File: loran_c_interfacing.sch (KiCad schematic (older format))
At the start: 17 parts, among them P401 SPI Bus A, P402 SPI Bus B, U103 74AC14, U401 74AC14, U402 74AC14

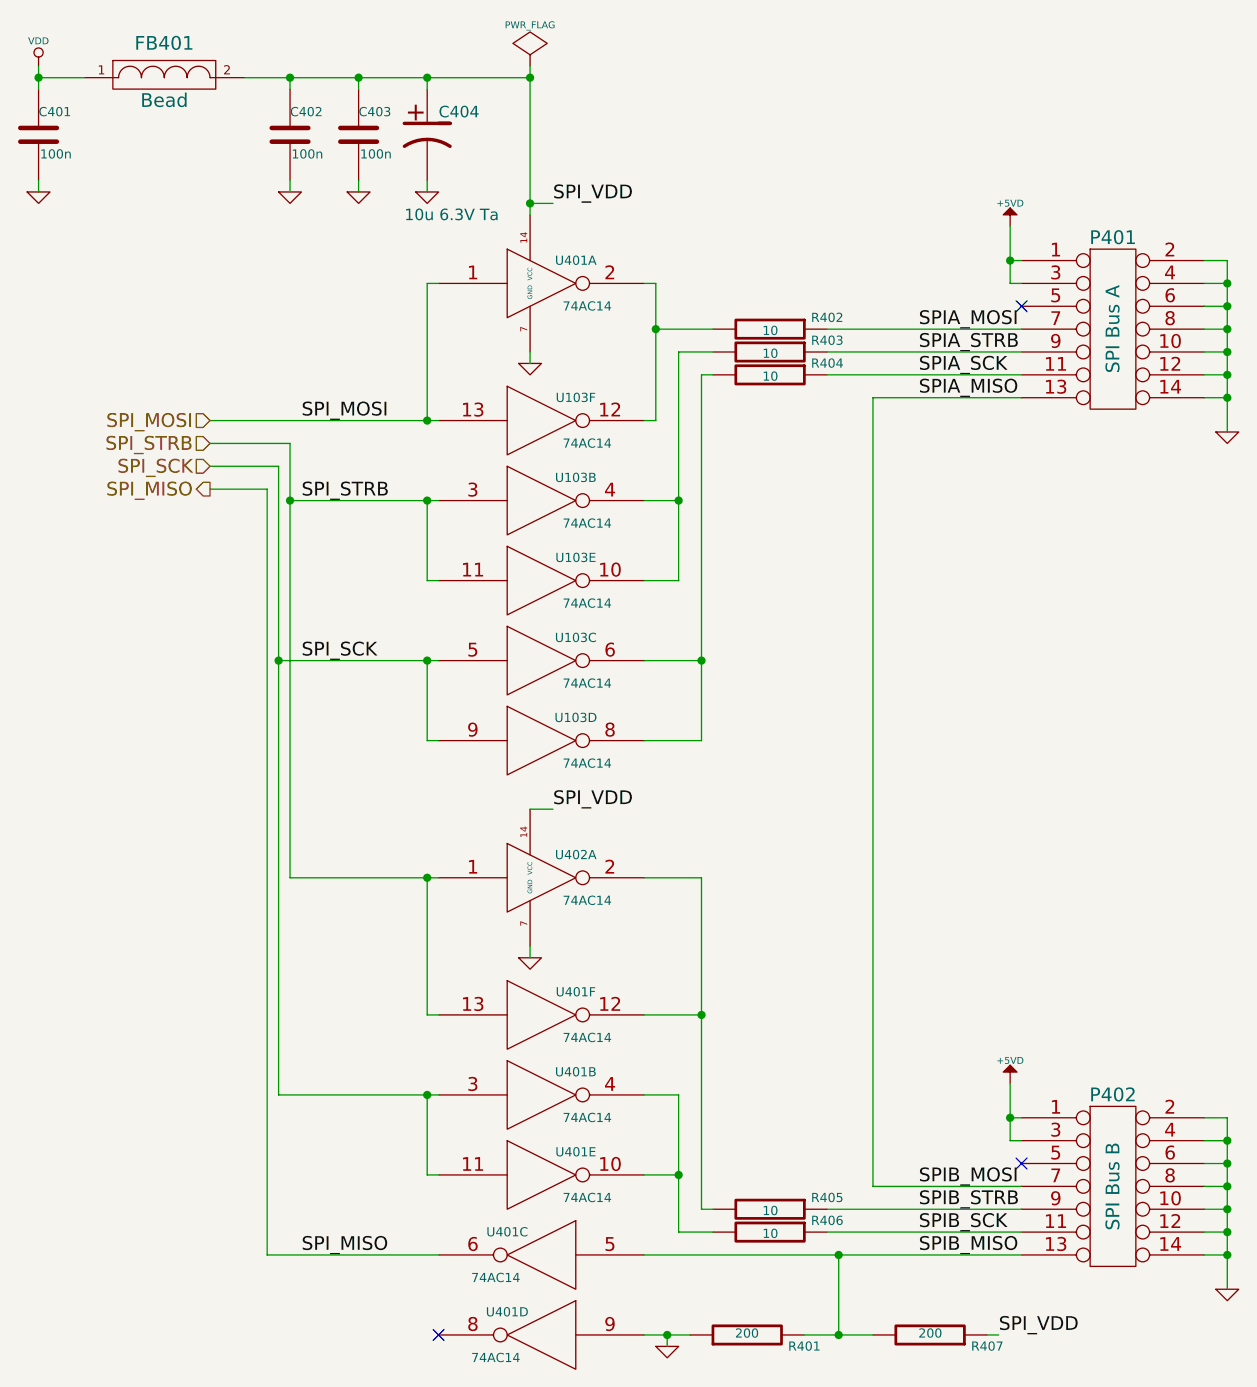
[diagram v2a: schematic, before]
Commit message: Fix: broken annotation, sheet numbers, incorrect 74AC14 package
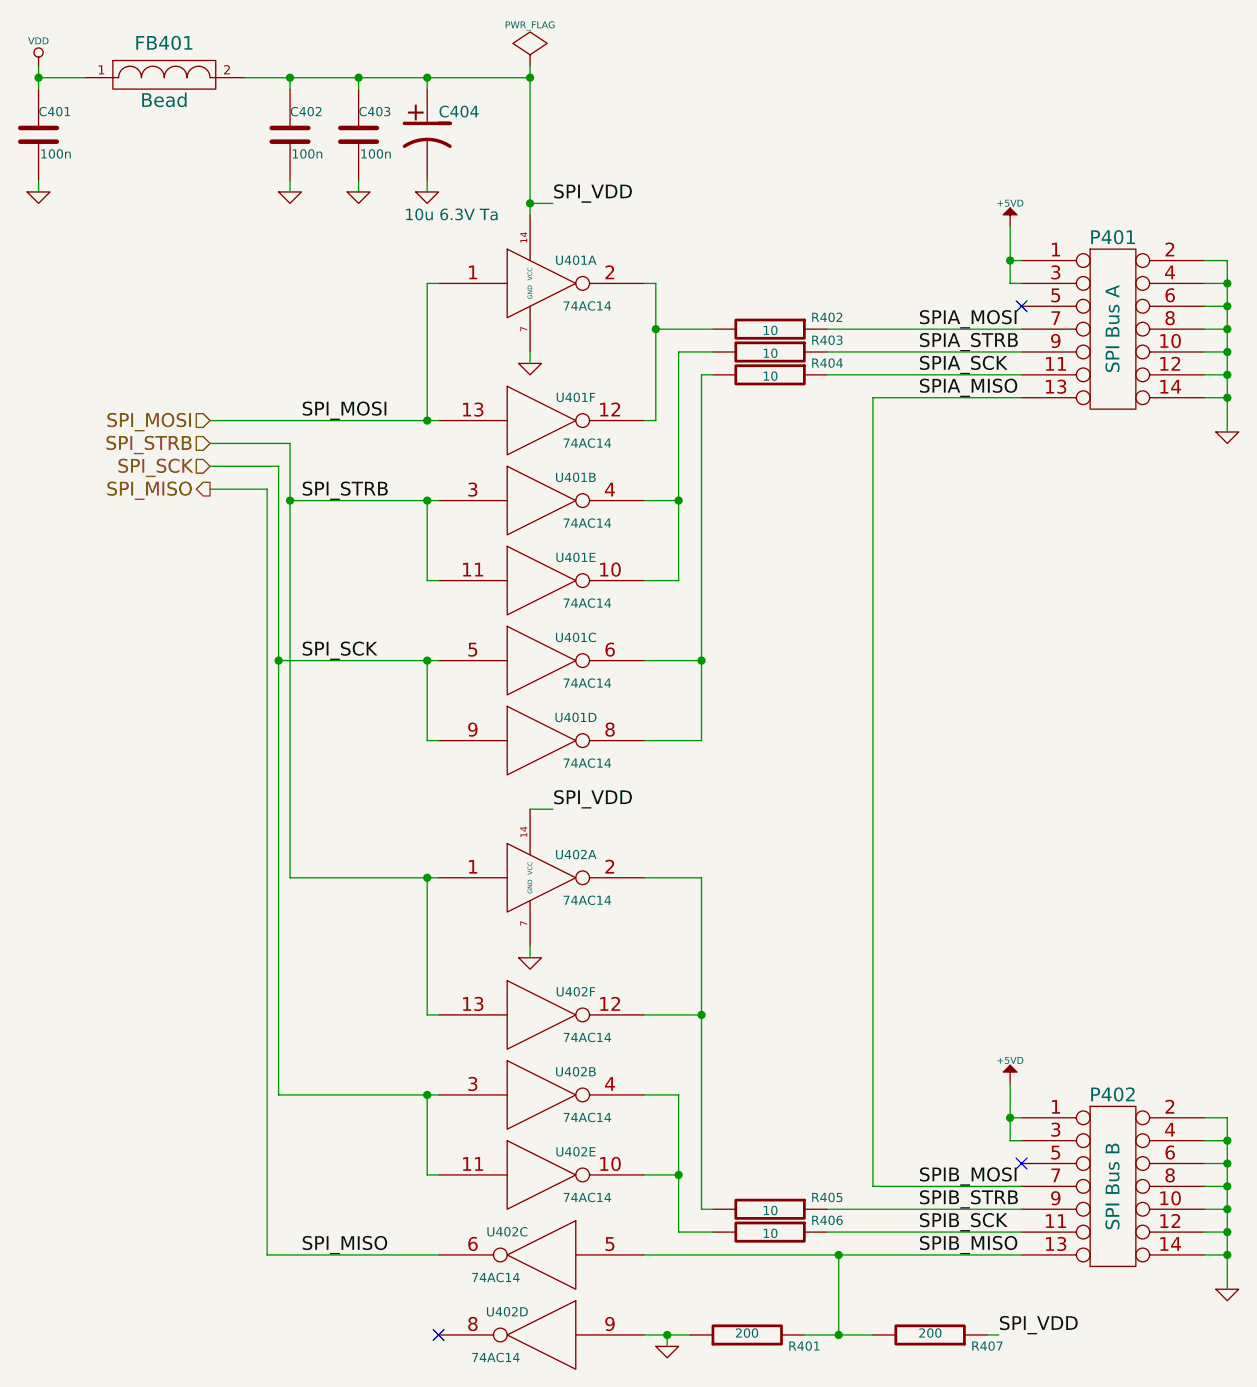
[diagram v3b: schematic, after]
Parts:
- renumbered U103 to U401, U401 to U402
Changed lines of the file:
@@
 $Descr A4 11693 8268
 encoding utf-8
-Sheet 3 7
+Sheet 4 7
 Title "SPI interface"
 Date ""
@@
 SPI_VDD
 $Comp
-L 74HC14 U103
+L 74HC14 U401
 U 6 1 52DD85CF
 P 5600 2300
-F 0 "U103" H 5750 2400 40  0000 C CNN
+F 0 "U401" H 5750 2400 40  0000 C CNN
 F 1 "74AC14" H 5800 2200 40  0000 C CNN
 F 2 "w_smd_dil:so-16" H 5600 2300 60  0001 C CNN
@@
 $EndComp
 $Comp
-L 74HC14 U103
+L 74HC14 U401
 U 2 1 52DD85E6
 P 5600 2650
-F 0 "U103" H 5750 2750 40  0000 C CNN
+F 0 "U401" H 5750 2750 40  0000 C CNN
 F 1 "74AC14" H 5800 2550 40  0000 C CNN
 F 2 "w_smd_dil:so-16" H 5600 2650 60  0001 C CNN
@@
 $EndComp
 $Comp
-L 74HC14 U103
+L 74HC14 U401
 U 5 1 52DD85F1
 P 5600 3000
-F 0 "U103" H 5750 3100 40  0000 C CNN
+F 0 "U401" H 5750 3100 40  0000 C CNN
 F 1 "74AC14" H 5800 2900 40  0000 C CNN
 F 2 "w_smd_dil:so-16" H 5600 3000 60  0001 C CNN
@@
 $EndComp
 $Comp
-L 74HC14 U103
+L 74HC14 U401
 U 3 1 52DD85FC
 P 5600 3350
-F 0 "U103" H 5750 3450 40  0000 C CNN
+F 0 "U401" H 5750 3450 40  0000 C CNN
 F 1 "74AC14" H 5800 3250 40  0000 C CNN
 F 2 "w_smd_dil:so-16" H 5600 3350 60  0001 C CNN
@@
 $EndComp
 $Comp
-L 74HC14 U103
+L 74HC14 U401
 U 4 1 52DD8607
 P 5600 3700
-F 0 "U103" H 5750 3800 40  0000 C CNN
+F 0 "U401" H 5750 3800 40  0000 C CNN
 F 1 "74AC14" H 5800 3600 40  0000 C CNN
 F 2 "w_smd_dil:so-16" H 5600 3700 60  0001 C CNN
@@
 SPI_VDD
 $Comp
-L 74HC14 U401
+L 74HC14 U402
 U 6 1 52DD8939
 P 5600 4900
-F 0 "U401" H 5750 5000 40  0000 C CNN
+F 0 "U402" H 5750 5000 40  0000 C CNN
 F 1 "74AC14" H 5800 4800 40  0000 C CNN
 F 2 "w_smd_dil:so-16" H 5600 4900 60  0001 C CNN
@@
 $EndComp
 $Comp
-L 74HC14 U401
+L 74HC14 U402
 U 2 1 52DD893F
 P 5600 5250
-F 0 "U401" H 5750 5350 40  0000 C CNN
+F 0 "U402" H 5750 5350 40  0000 C CNN
 F 1 "74AC14" H 5800 5150 40  0000 C CNN
 F 2 "w_smd_dil:so-16" H 5600 5250 60  0001 C CNN
@@
 $EndComp
 $Comp
-L 74HC14 U401
+L 74HC14 U402
 U 5 1 52DD8945
 P 5600 5600
-F 0 "U401" H 5750 5700 40  0000 C CNN
+F 0 "U402" H 5750 5700 40  0000 C CNN
 F 1 "74AC14" H 5800 5500 40  0000 C CNN
 F 2 "w_smd_dil:so-16" H 5600 5600 60  0001 C CNN
@@
 $EndComp
 $Comp
-L 74HC14 U401
+L 74HC14 U402
 U 3 1 52DD894B
 P 5600 5950
-F 0 "U401" H 5750 6050 40  0000 C CNN
+F 0 "U402" H 5750 6050 40  0000 C CNN
 F 1 "74AC14" H 5800 5850 40  0000 C CNN
 F 2 "w_smd_dil:so-16" H 5600 5950 60  0001 C CNN
@@
 $EndComp
 $Comp
-L 74HC14 U401
+L 74HC14 U402
 U 4 1 52DD8951
 P 5600 6300
-F 0 "U401" H 5750 6400 40  0000 C CNN
+F 0 "U402" H 5750 6400 40  0000 C CNN
 F 1 "74AC14" H 5800 6200 40  0000 C CNN
 F 2 "w_smd_dil:so-16" H 5600 6300 60  0001 C CNN
